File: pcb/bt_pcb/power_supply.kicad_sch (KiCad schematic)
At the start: 37 parts, among them IC12 ADPL16000BATA+, IC13 LM3940IMP-3.3_NOPB, IC14 TLV76150DCYR, IC8 ADPL16000BATA+, IC9 LM3940IMP-3.3_NOPB, J1 Jack-DC, J6 Jack-DC

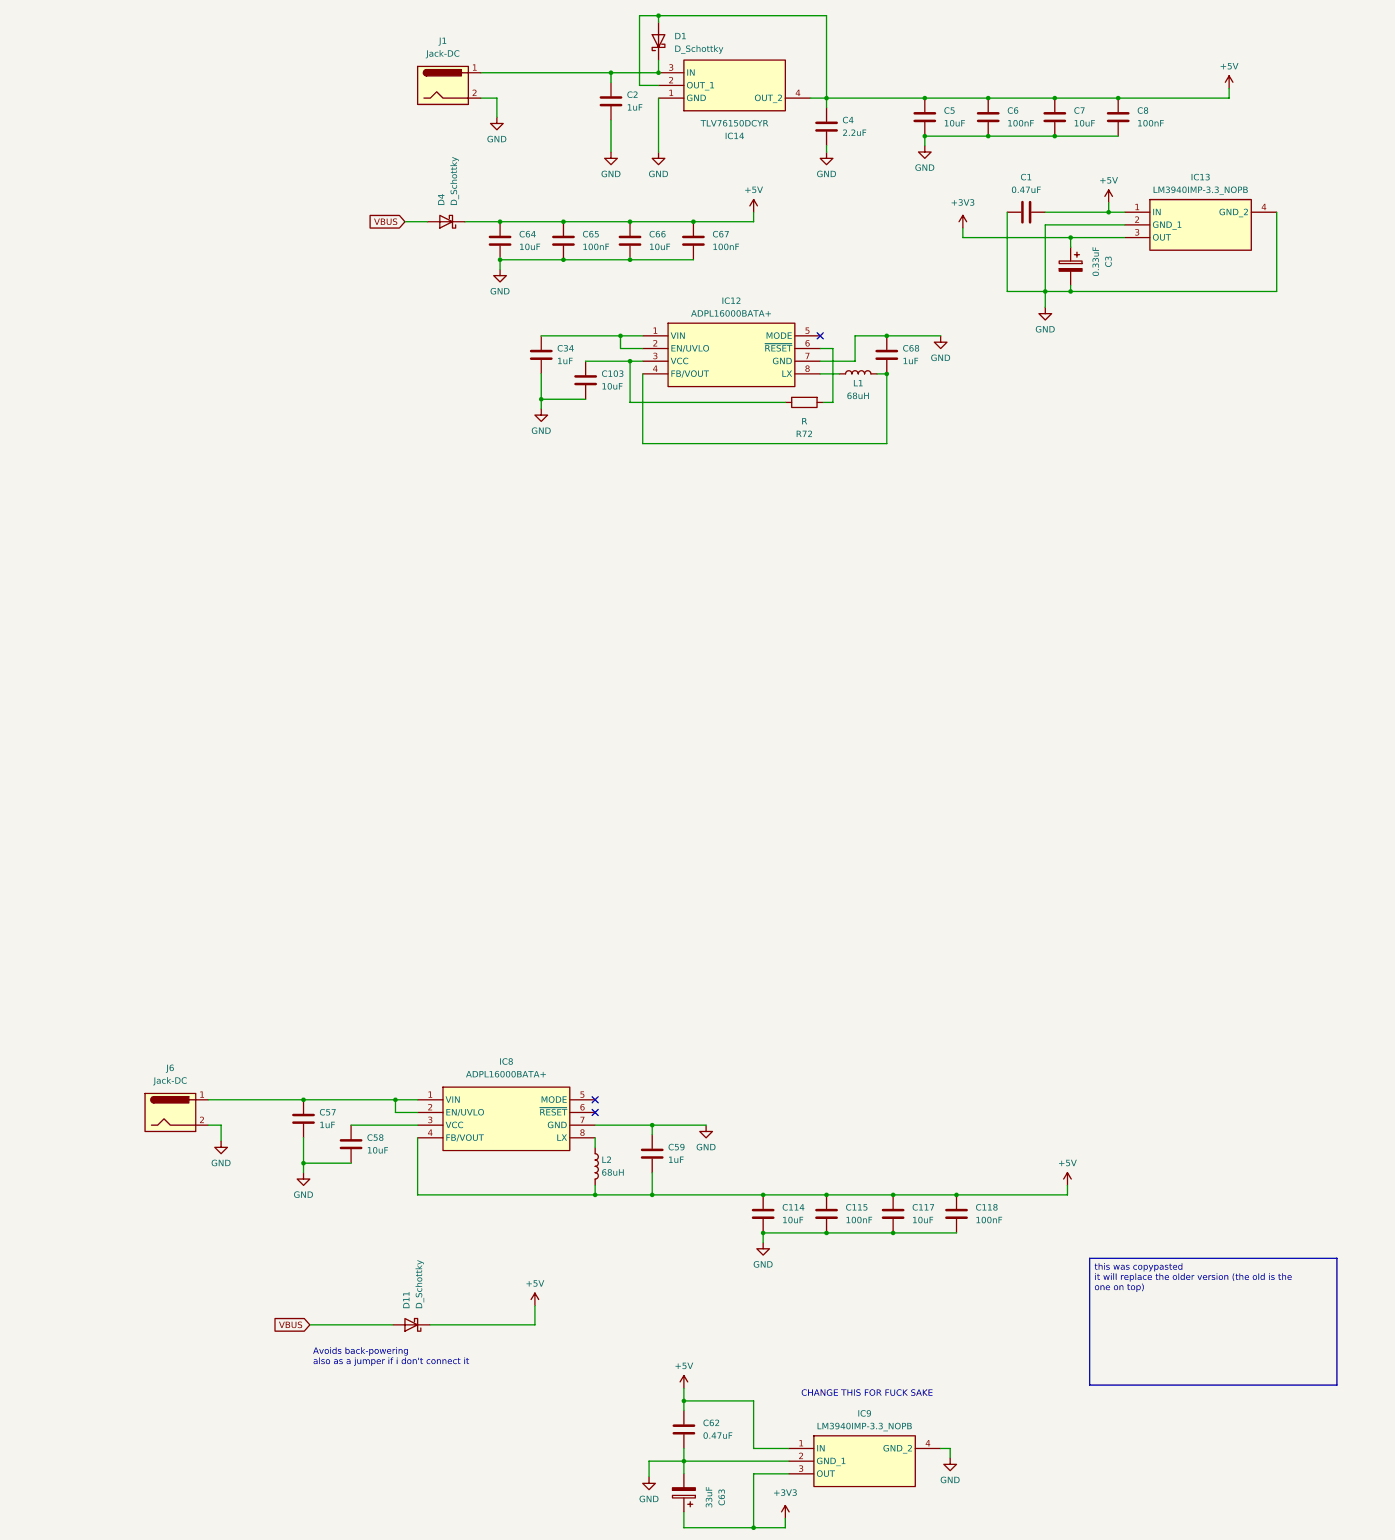
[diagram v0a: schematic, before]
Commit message: complete makeover of power supply
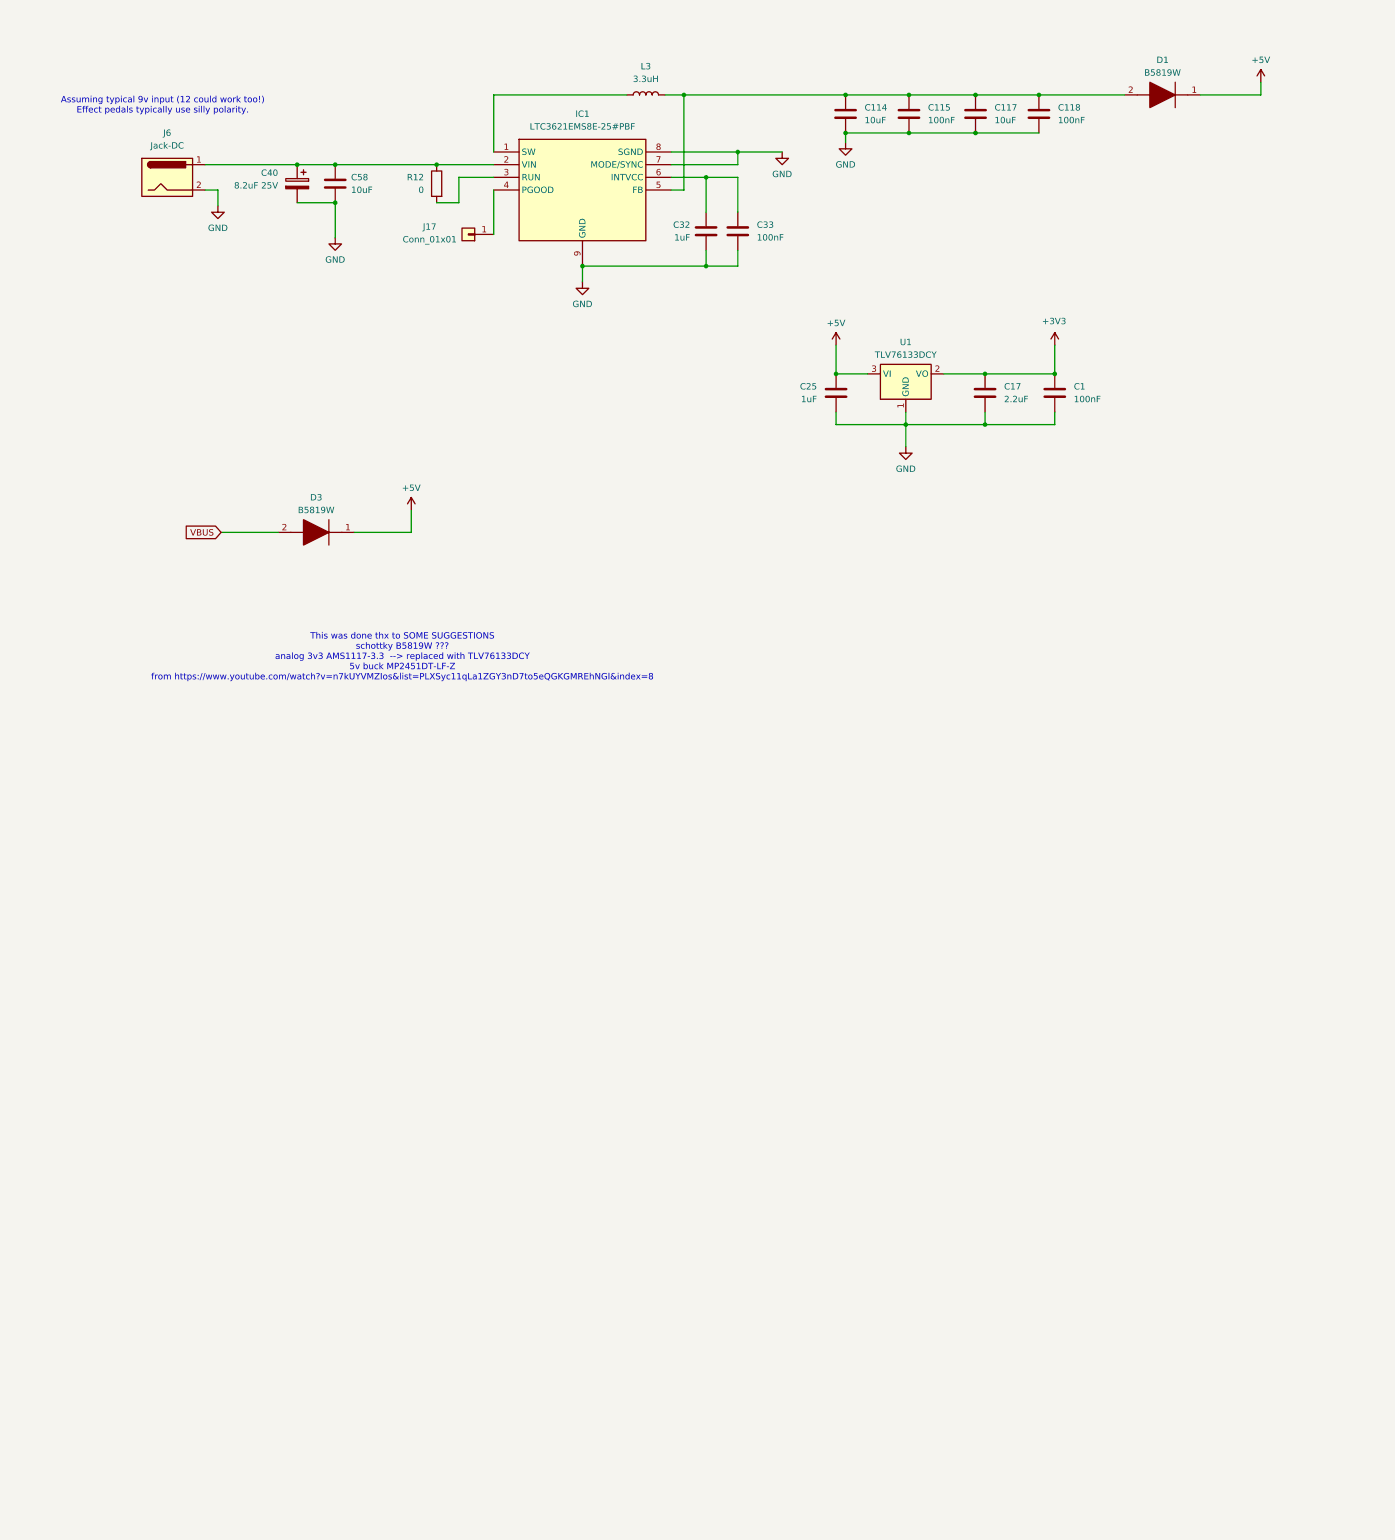
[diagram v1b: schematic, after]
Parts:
- removed C103, C5, C64, C66, C7: 10uF, symbol Device:C
- removed C2, C34, C68: 1uF, symbol Device:C
- removed C3: 0.33uF, symbol Device:C_Polarized
- removed C4: 2.2uF, symbol Device:C
- removed C57, C59: 1uF, Capacitor_SMD:C_0603_1608Metric, symbol Device:C
- removed C6, C65, C67, C8: 100nF, symbol Device:C
- removed C62: 0.47uF, Capacitor_SMD:C_0603_1608Metric, symbol Device:C
- removed C63: 33uF, Capacitor_SMD:C_0603_1608Metric, symbol Device:C_Polarized
- removed D1, D4: D_Schottky, symbol Device:D_Schottky
- removed D11: D_Schottky, Diode_SMD:D_0603_1608Metric, symbol Device:D_Schottky
- removed IC12, IC8: ADPL16000BATA+, library:ADPL16000BATA, symbol library:ADPL16000BATA+
- removed IC13, IC9: LM3940IMP-3.3_NOPB, library:SOT230P700X180-4N, symbol library:LM3940IMP-3.3_NOPB
- removed IC14: TLV76150DCYR, library:SOT230P700X180-4N, symbol library:TLV76150DCYR
- removed J1: Jack-DC, symbol Connector:Jack-DC
- removed L1: 68uH, symbol Device:L
- removed L2: 68uH, Inductor_SMD:L_12x12mm_H6mm, symbol Device:L
- removed R72: R, symbol Device:R
- added C17: 2.2uF, Capacitor_SMD:C_0603_1608Metric, symbol Device:C
- added C25, C32: 1uF, Capacitor_SMD:C_0603_1608Metric, symbol Device:C
- added C33: 100nF, Capacitor_SMD:C_0603_1608Metric, symbol Device:C
- added C40: 8.2uF 25V, symbol Device:C_Polarized
- added D1, D3: B5819W, SOD3716X125N, symbol library:B5819W
- added IC1: LTC3621EMS8E-25#PBF, SOP65P490X110-9N, symbol library:LTC3621EMS8E-25#PBF
- added J17: Conn_01x01, symbol Connector_Generic:Conn_01x01
- added L3: 3.3uH, Inductor_SMD:L_12x12mm_H6mm, symbol Device:L
- added R12: 0, symbol Device:R
- added U1: TLV76133DCY, Package_TO_SOT_SMD:SOT-223-3_TabPin2, symbol Regulator_Linear:TLV76133DCY
- C1: value 0.47uF -> 100nF; footprint (none) -> Capacitor_SMD:C_0603_1608Metric
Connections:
- net +3V3: now also C1.1, C17.2, U1.2 (VO)
- net +5V: now also C25.2, D1.1 (K), D3.1 (K), U1.3 (VI); no longer C1.2, C114.1, C115.1, C117.1, C118.1
- net GND: now also C1.2, C17.1, C25.1, C32.2, C33.2, C40.2, IC1.7 (MODE/SYNC), IC1.8 (SGND), IC1.9 (GND), U1.1 (GND); no longer C1.1
- net VBUS: now also D3.2 (A)
- net at J6.1: now also C58.1, C40.1, IC1.2 (VIN), R12.1
- new net: C114.1, C115.1, C117.1, C118.1, D1.2 (A), IC1.5 (FB), L3.2
- new net: IC1.4 (PGOOD), J17.1 (Pin_1)
- new net: C32.1, C33.1, IC1.6 (INTVCC)
- new net: IC1.3 (RUN), R12.2
- new net: IC1.1 (SW), L3.1
- no-connect marks 3 -> 0
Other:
- note added: "Assuming typical 9v input (12 could work too!) Effect pedals typically use silly polarity."
- note added: "This was done thx to SOME SUGGESTIONS schottky B5819W ??? analog 3v3 AMS1117-3.3 --> replaced with TLV76133DCY 5v buck MP2451DT-LF-Z from https://www.youtube.com/watch?v=n7kUYVMZIos&list=PLXSyc11qLa1ZGY3nD7to5eQGKGMREhNGl&index=8"
- note removed: "Avoids back-powering also as a jumper if i don't connect it"
- note removed: "CHANGE THIS FOR FUCK SAKE"
- moved on the sheet: C114, C115, C117, C118, C58, J6

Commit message: big progress, now revising error and warnings
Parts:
- added C21: 100nF, Capacitor_SMD:C_0603_1608Metric, symbol Device:C
- added C7: 1uF, Capacitor_SMD:C_0603_1608Metric, symbol Device:C
- added C8: 2.2uF, Capacitor_SMD:C_0603_1608Metric, symbol Device:C
- added U2: TLV76133DCY, Package_TO_SOT_SMD:SOT-223-3_TabPin2, symbol Regulator_Linear:TLV76133DCY
- D1, D3: footprint SOD3716X125N -> library:SOD3716X125N
- IC1: footprint SOP65P490X110-9N -> library:SOP65P490X110-9N
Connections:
- net +5V: now also C7.2, U2.3 (VI)
- net GND: now also C21.2, C7.1, C8.1, U2.1 (GND)
- new net +3V3A: C21.1, C8.2, U2.2 (VO)
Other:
- moved on the sheet: L3

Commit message: solving some erc warnings and errors
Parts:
- renumbered C40 to C1, C17 to C10, C8 to C11, C118 to C12, C1 to C13, C21 to C14, C58 to C2, C32 to C3, C33 to C4, C25 to C5, C7 to C6, C114 to C7, C115 to C8, C117 to C9, D3 to D1, D1 to D2, J6 to J1, J17 to J2, L3 to L1, R12 to R1
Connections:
- net +3V3A renamed +3.3VA
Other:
- moved on the sheet: C1, C10, C11, C12, C13, C14, C2, C3, C4, C5, C6, C7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

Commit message: schematic in theory finished
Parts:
- removed C1: 8.2uF 25V, symbol Device:C_Polarized
- added C5: 10u, Capacitor_SMD:C_0805_2012Metric_Pad1.18x1.45mm_HandSolder, symbol Device:C
- C1: renamed from C7; value 10uF -> 10u; footprint Capacitor_SMD:C_0603_1608Metric -> Capacitor_SMD:C_0805_2012Metric_Pad1.18x1.45mm_HandSolder
- C10: value 2.2uF -> 2.2u; footprint Capacitor_SMD:C_0603_1608Metric -> Capacitor_SMD:C_0603_1608Metric_Pad1.08x0.95mm_HandSolder
- C11: renamed from C13; value 100nF -> 100n; footprint Capacitor_SMD:C_0603_1608Metric -> Capacitor_SMD:C_0603_1608Metric_Pad1.08x0.95mm_HandSolder
- C12: renamed from C6; value 1uF -> 1u; footprint Capacitor_SMD:C_0603_1608Metric -> Capacitor_SMD:C_0603_1608Metric_Pad1.08x0.95mm_HandSolder
- C13: renamed from C11; value 2.2uF -> 2.2u; footprint Capacitor_SMD:C_0603_1608Metric -> Capacitor_SMD:C_0603_1608Metric_Pad1.08x0.95mm_HandSolder
- C14: value 100nF -> 100n; footprint Capacitor_SMD:C_0603_1608Metric -> Capacitor_SMD:C_0603_1608Metric_Pad1.08x0.95mm_HandSolder
- C2: renamed from C8; value 100nF -> 100n; footprint Capacitor_SMD:C_0603_1608Metric -> Capacitor_SMD:C_0603_1608Metric_Pad1.08x0.95mm_HandSolder
- C3: renamed from C9; value 10uF -> 10u; footprint Capacitor_SMD:C_0603_1608Metric -> Capacitor_SMD:C_0805_2012Metric_Pad1.18x1.45mm_HandSolder
- C4: renamed from C12; value 100nF -> 100n; footprint Capacitor_SMD:C_0603_1608Metric -> Capacitor_SMD:C_0603_1608Metric_Pad1.08x0.95mm_HandSolder
- C6: renamed from C2; value 10uF -> 10u; footprint Capacitor_SMD:C_0603_1608Metric -> Capacitor_SMD:C_0805_2012Metric_Pad1.18x1.45mm_HandSolder
- C7: renamed from C3; value 1uF -> 1u; footprint Capacitor_SMD:C_0603_1608Metric -> Capacitor_SMD:C_0603_1608Metric_Pad1.08x0.95mm_HandSolder
- C8: renamed from C4; value 100nF -> 100n; footprint Capacitor_SMD:C_0603_1608Metric -> Capacitor_SMD:C_0603_1608Metric_Pad1.08x0.95mm_HandSolder
- C9: renamed from C5; value 1uF -> 1u; footprint Capacitor_SMD:C_0603_1608Metric -> Capacitor_SMD:C_0603_1608Metric_Pad1.08x0.95mm_HandSolder
- J2: footprint (none) -> Connector_PinHeader_2.54mm:PinHeader_1x01_P2.54mm_Vertical
- L1: value 3.3uH -> 3.3u; footprint Inductor_SMD:L_12x12mm_H6mm -> Inductor_SMD:L_1008_2520Metric_Pad1.43x2.20mm_HandSolder
- R1: footprint (none) -> Resistor_SMD:R_0603_1608Metric_Pad0.98x0.95mm_HandSolder
- renumbered D2 to D1, D1 to D2
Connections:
- net GND: now also C5.2
- net at C6.1, IC1.2 (VIN), J1.1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: now also C5.1
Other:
- note added: "DFE252012PD-3R3M=P2 1008 (2520 metric)"

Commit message: pcb started
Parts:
- removed J1: Jack-DC, Connector_BarrelJack:BarrelJack_Wuerth_6941xx301002, symbol Connector:Jack-DC
- added J1: Conn_01x02, Connector_PinHeader_2.54mm:PinHeader_1x02_P2.54mm_Vertical, symbol Connector_Generic:Conn_01x02
- added J2: 694106301002, library:694106301002_1, symbol library:694106301002
- added R1: 10k, Resistor_SMD:R_0603_1608Metric_Pad0.98x0.95mm_HandSolder, symbol Device:R
- renumbered J2 to J3, R1 to R2
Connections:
- net GND: now also J1.1 (Pin_1), J2.1 (POWER), R1.2
- net at C5.1, C6.1, IC1.2 (VIN)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: now also J1.2 (Pin_2), J2.2 (GND_1)
- new net: J2.3 (GND_2), R1.1

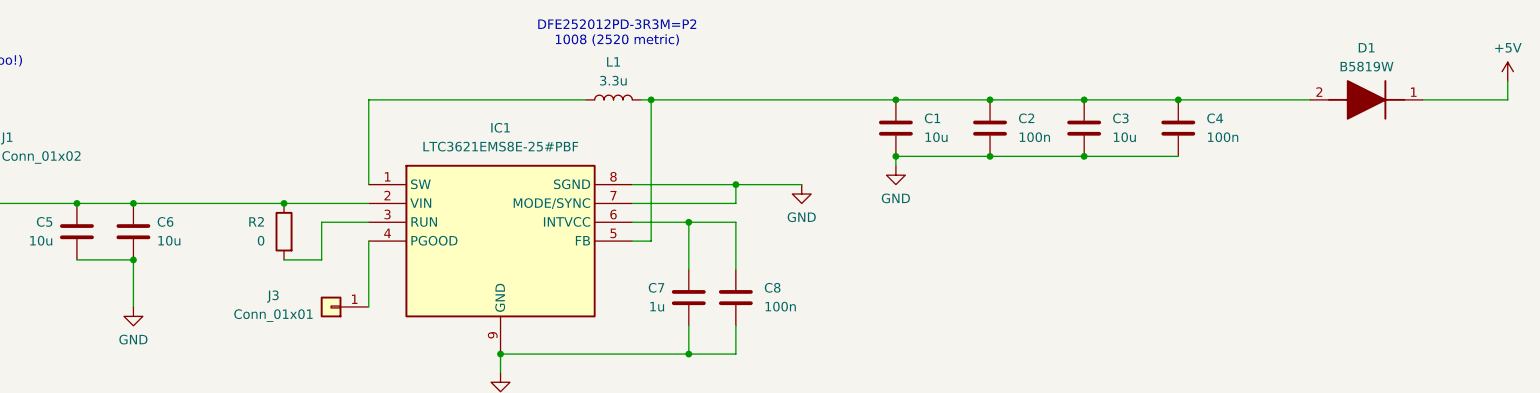
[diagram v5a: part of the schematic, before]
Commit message: pcb with some schematic tuning
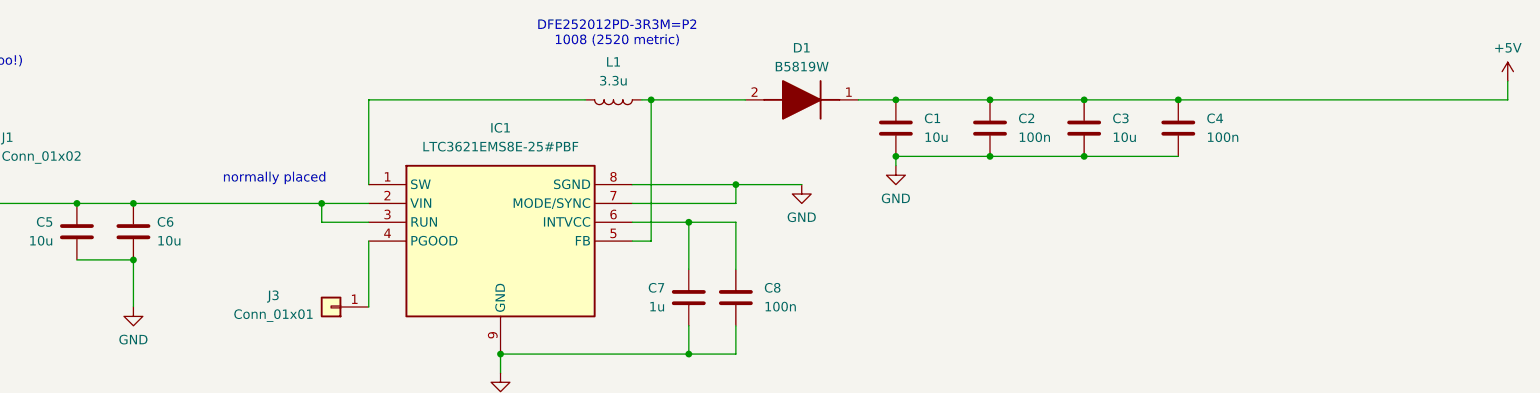
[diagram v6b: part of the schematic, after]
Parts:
- removed R2: 0, Resistor_SMD:R_0603_1608Metric_Pad0.98x0.95mm_HandSolder, symbol Device:R
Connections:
- net +5V: now also C1.1, C2.1, C3.1, C4.1
- net at C5.1, C6.1, IC1.2 (VIN)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: now also IC1.3 (RUN)
- net at L1.1: now also D1.2 (A), IC1.5 (FB); no longer IC1.1 (SW)
- new net: IC1.1 (SW), L1.2
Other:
- note added: "normally placed"
- moved on the sheet: D1, L1
